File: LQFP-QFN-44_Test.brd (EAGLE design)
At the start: 37.8 x 25.4 mm, 10 parts, among them SW1 101-0134-EV, U1 P8X32A, X1 ATS060CSM-1

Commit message: Changed Crystal Value to ABLS3-6.000MHZ-D4Y-T
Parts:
- X1: value ATS060CSM-1 -> ABLS3-6.000MHZ-D4Y-T
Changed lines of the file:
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@@
 <attribute name="NAME" x="13.497" y="20.1295" size="0.8128" layer="25" font="vector"/>
 </element>
-<element name="X1" library="PP_FreqCtrl" package="HC-49/US_SM" value="ATS060CSM-1" x="31.242" y="12.954" smashed="yes" rot="R90">
+<element name="X1" library="PP_FreqCtrl" package="HC-49/US_SM" value="ABLS3-6.000MHZ-D4Y-T" x="31.242" y="12.954" smashed="yes" rot="R90">
 <attribute name="NAME" x="28.702" y="18.796" size="0.8128" layer="21" font="vector"/>
 </element>

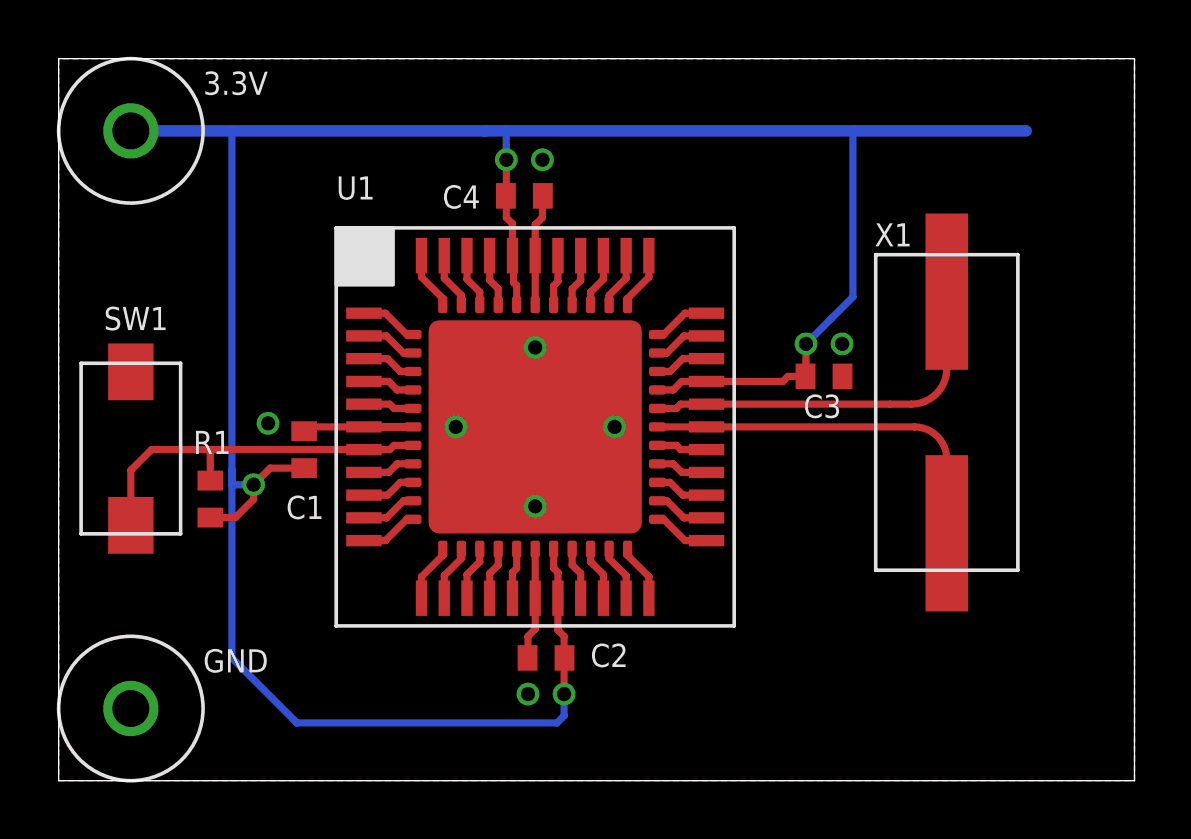
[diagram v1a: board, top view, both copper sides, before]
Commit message: Fixed GND trace near XTAL pin.
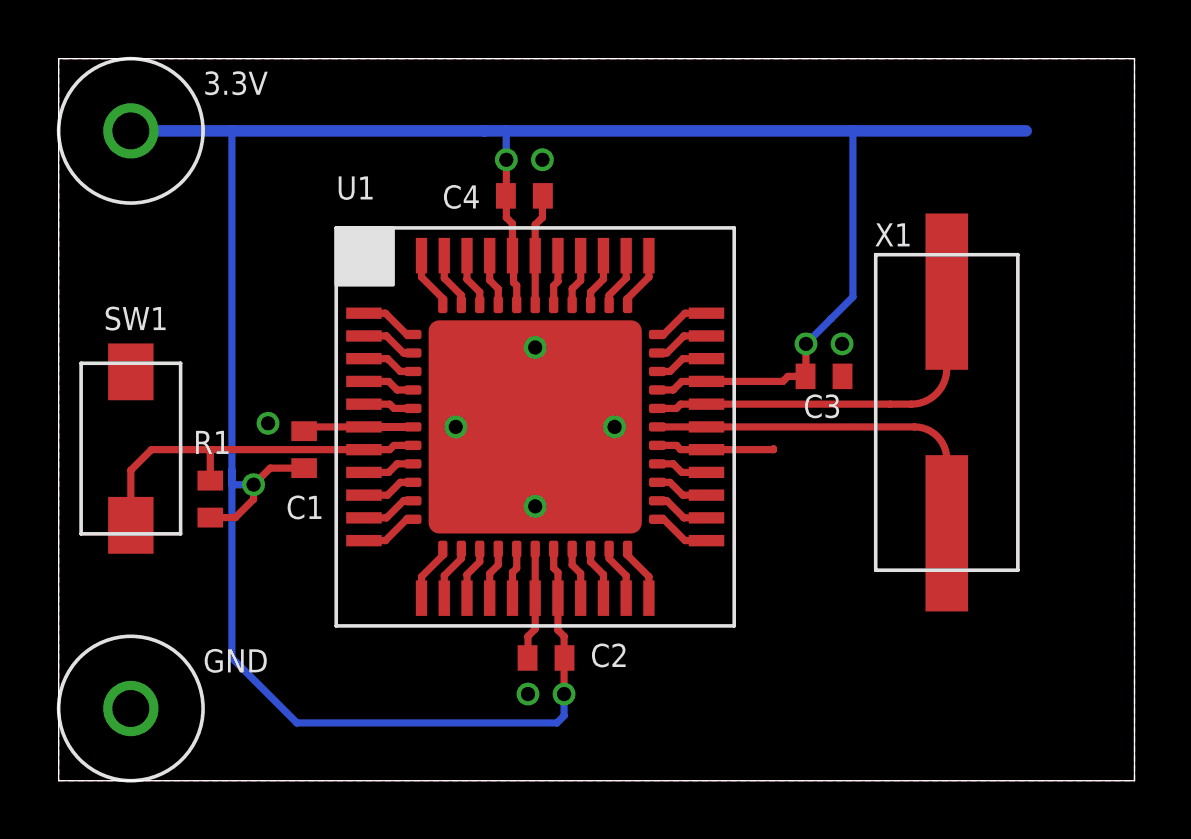
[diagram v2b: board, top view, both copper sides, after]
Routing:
- net GND: track 17.1 -> 19.6 mm
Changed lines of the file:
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@@
 <?xml version="1.0" encoding="utf-8"?>
 <!DOCTYPE eagle SYSTEM "eagle.dtd">
-<eagle version="6.3">
+<eagle version="6.5.0">
 <drawing>
 <settings>
@@
 <wire x1="21.064" y1="11.796" x2="21.732" y2="11.796" width="0.254" layer="1"/>
 <wire x1="21.732" y1="11.796" x2="21.882" y2="11.646" width="0.254" layer="1"/>
-<wire x1="22.789" y1="11.646" x2="21.882" y2="11.646" width="0.254" layer="1"/>
 <contactref element="U1" pad="6"/>
 <contactref element="U1" pad="50"/>
@@
 <via x="17.018" y="21.844" extent="1-16" drill="0.5"/>
 <via x="16.51" y="3.048" extent="1-16" drill="0.5"/>
+<wire x1="22.789" y1="11.646" x2="25.146" y2="11.646" width="0.254" layer="1"/>
+<wire x1="25.146" y1="11.646" x2="25.146" y2="11.684" width="0.254" layer="1"/>
+<wire x1="21.882" y1="11.646" x2="22.86" y2="11.646" width="0.254" layer="1"/>
+<wire x1="22.86" y1="11.646" x2="22.86" y2="11.684" width="0.254" layer="1"/>
 </signal>
 <signal name="P16">
